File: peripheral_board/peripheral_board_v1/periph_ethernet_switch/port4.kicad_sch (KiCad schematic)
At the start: 7 parts, among them J4 0826-1G1T-23-F

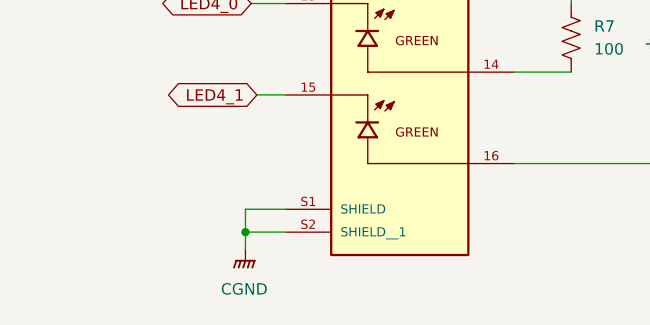
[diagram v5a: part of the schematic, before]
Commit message: Switch PCB layout done
The layout should be done. there are a lot of DRC errors but it seems like it is all for things like through holes and other similar items are causing this.
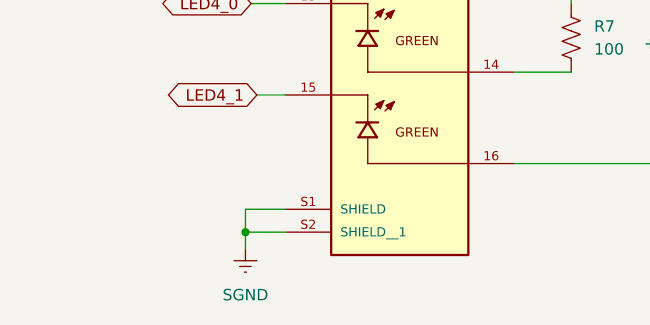
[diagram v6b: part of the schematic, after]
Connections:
- net CGND is gone; now on net SGND: J4.S1 (SHIELD), J4.S2 (SHIELD__1)
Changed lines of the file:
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@@
+	(symbol
+		(lib_id "power:GNDREF")
+		(at 42.545 87.63 0)
+		(unit 1)
+		(exclude_from_sim no)
+		(in_bom yes)
+		(on_board yes)
+		(dnp no)
+		(property "Reference" "#PWR028"
+			(at 42.545 93.98 0)
+			(effects
+				(font
+					(size 1.27 1.27)
+				)
+				(hide yes)
+			)
+		)
+		(property "Value" "SGND"
+			(at 42.545 92.71 0)
+			(effects
+				(font
+					(size 1.27 1.27)
+				)
+			)
+		)
+		(property "Footprint" ""
+			(at 42.545 87.63 0)
+			(effects
+				(font
+					(size 1.27 1.27)
+				)
+				(hide yes)
+			)
+		)
+		(property "Datasheet" ""
+			(at 42.545 87.63 0)
+			(effects
+				(font
+					(size 1.27 1.27)
+				)
+				(hide yes)
+			)
+		)
+		(property "Description" "Power symbol creates a global label with name \"GNDREF\" , reference supply ground"
+			(at 42.545 87.63 0)
+			(effects
+				(font
+					(size 1.27 1.27)
+				)
+				(hide yes)
+			)
+		)
+		(pin "1"
+		)
+		(instances
+			(project "periph_ethernet_switch"
+				(path "/065aff9d-de72-4d05-9bf8-aade8202d5c4/c3ca900e-99ac-4769-98db-f2b6577cf32c"
+					(reference "#PWR028")
+					(unit 1)
+				)
+			)
+		)
+	)
 	(symbol
 		(lib_id "power:GNDREF")
@@
 					(unit 1)
 				)
-			)
-		)
-	)
-	(symbol
-		(lib_id "power:GNDPWR")
-		(at 42.545 87.63 0)
-		(unit 1)
-		(exclude_from_sim no)
-		(in_bom yes)
-		(on_board yes)
-		(dnp no)
-		(fields_autoplaced yes)
-		(property "Reference" "#PWR035"
-			(at 42.545 92.71 0)
-			(effects
-				(font
-					(size 1.27 1.27)
-				)
-				(hide yes)
-			)
-		)
-		(property "Value" "CGND"
-			(at 42.418 92.075 0)
-			(effects
-				(font
-					(size 1.27 1.27)
-				)
-			)
-		)
-		(property "Footprint" ""
-			(at 42.545 88.9 0)
-			(effects
-				(font
-					(size 1.27 1.27)
-				)
-				(hide yes)
-			)
-		)
-		(property "Datasheet" ""
-			(at 42.545 88.9 0)
-			(effects
-				(font
-					(size 1.27 1.27)
-				)
-				(hide yes)
-			)
-		)
-		(property "Description" "Power symbol creates a global label with name \"CGND\" , CHASSIS GND"
-			(at 42.545 87.63 0)
-			(effects
-				(font
-					(size 1.27 1.27)
-				)
-				(hide yes)
-			)
-		)
-		(pin "1"
-		)
-		(instances
-			(project "periph_ethernet_switch"
-				(path "/065aff9d-de72-4d05-9bf8-aade8202d5c4/c3ca900e-99ac-4769-98db-f2b6577cf32c"
-					(reference "#PWR035")
-					(unit 1)
-				)

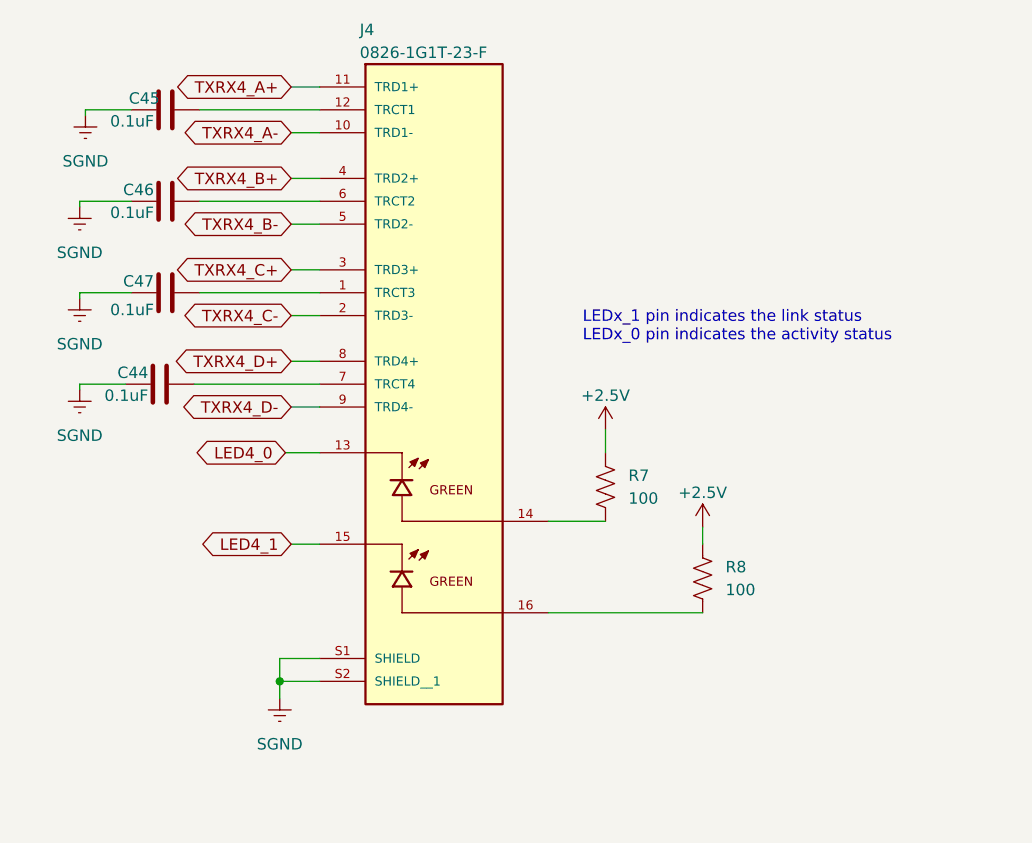
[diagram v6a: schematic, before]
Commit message: WIP for new switch
Made some minor changes which are detailed in Notion.
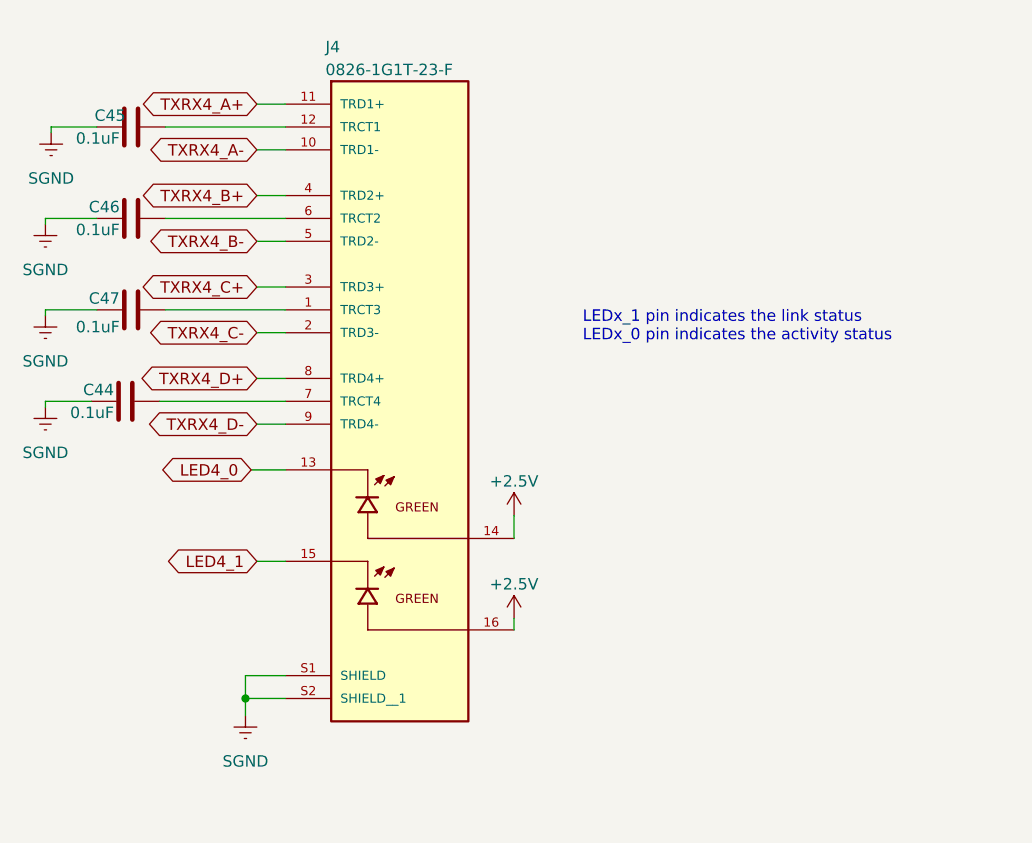
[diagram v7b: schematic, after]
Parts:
- removed R7, R8: 100, Resistor_SMD:R_0603_1608Metric, symbol Device:R_US
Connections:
- net +2.5V: now also J4.14, J4.16
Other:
- moved on the sheet: C44, C45, C46, C47, J4

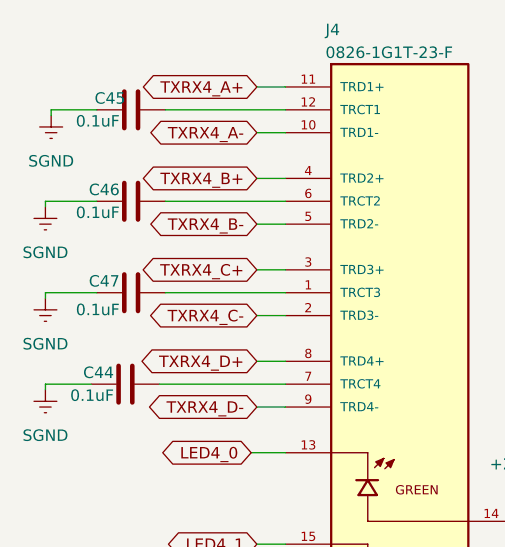
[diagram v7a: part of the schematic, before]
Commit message: Changes to the board layout
Need to finish doing some layout but waiting on Microchip to confirm with what I have. Might want to change the EDA symbol for the switch IC.
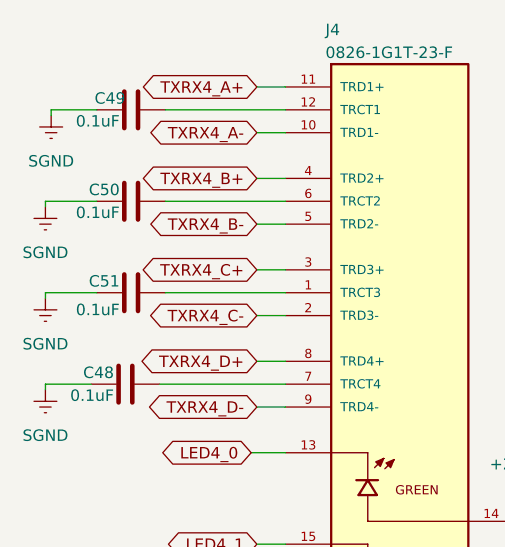
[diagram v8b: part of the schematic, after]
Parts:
- renumbered C44 to C48, C45 to C49, C46 to C50, C47 to C51
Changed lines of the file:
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@@
 		(on_board yes)
 		(dnp no)
-		(property "Reference" "#PWR033"
+		(property "Reference" "#PWR081"
 			(at 16.51 61.595 0)
 			(effects
@@
 			(project "periph_ethernet_switch"
 				(path "/065aff9d-de72-4d05-9bf8-aade8202d5c4/c3ca900e-99ac-4769-98db-f2b6577cf32c"
-					(reference "#PWR033")
+					(reference "#PWR081")
 					(unit 1)
 				)
@@
 		(on_board yes)
 		(dnp no)
-		(property "Reference" "C45"
+		(property "Reference" "C49"
 			(at 25.4 22.86 90)
 			(effects
@@
 			(project "periph_ethernet_switch"
 				(path "/065aff9d-de72-4d05-9bf8-aade8202d5c4/c3ca900e-99ac-4769-98db-f2b6577cf32c"
-					(reference "C45")
+					(reference "C49")
 					(unit 1)
 				)
@@
 		(on_board yes)
 		(dnp no)
-		(property "Reference" "C46"
+		(property "Reference" "C50"
 			(at 24.765 33.02 90)
 			(effects
@@
 			(project "periph_ethernet_switch"
 				(path "/065aff9d-de72-4d05-9bf8-aade8202d5c4/c3ca900e-99ac-4769-98db-f2b6577cf32c"
-					(reference "C46")
+					(reference "C50")
 					(unit 1)
 				)
@@
 		(on_board yes)
 		(dnp no)
-		(property "Reference" "#PWR028"
+		(property "Reference" "#PWR083"
 			(at 38.735 95.885 0)
 			(effects
@@
 			(project "periph_ethernet_switch"
 				(path "/065aff9d-de72-4d05-9bf8-aade8202d5c4/c3ca900e-99ac-4769-98db-f2b6577cf32c"
-					(reference "#PWR028")
+					(reference "#PWR083")
 					(unit 1)
 				)
@@
 		(on_board yes)
 		(dnp no)
-		(property "Reference" "#PWR034"
+		(property "Reference" "#PWR082"
 			(at 17.145 31.115 0)
 			(effects
@@
 			(project "periph_ethernet_switch"
 				(path "/065aff9d-de72-4d05-9bf8-aade8202d5c4/c3ca900e-99ac-4769-98db-f2b6577cf32c"
-					(reference "#PWR034")
+					(reference "#PWR082")
 					(unit 1)
 				)
@@
 		(on_board yes)
 		(dnp no)
-		(property "Reference" "#PWR031"
+		(property "Reference" "#PWR079"
 			(at 16.51 41.275 0)
 			(effects
@@
 			(project "periph_ethernet_switch"
 				(path "/065aff9d-de72-4d05-9bf8-aade8202d5c4/c3ca900e-99ac-4769-98db-f2b6577cf32c"
-					(reference "#PWR031")
+					(reference "#PWR079")
 					(unit 1)
 				)
@@
 		(on_board yes)
 		(dnp no)
-		(property "Reference" "C47"
+		(property "Reference" "C51"
 			(at 24.765 43.18 90)
 			(effects
@@
 			(project "periph_ethernet_switch"
 				(path "/065aff9d-de72-4d05-9bf8-aade8202d5c4/c3ca900e-99ac-4769-98db-f2b6577cf32c"
-					(reference "C47")
+					(reference "C51")
 					(unit 1)
 				)
@@
 		(on_board yes)
 		(dnp no)
-		(property "Reference" "#PWR036"
+		(property "Reference" "#PWR084"
 			(at 68.58 71.12 0)
 			(effects
@@
 			(project "periph_ethernet_switch"
 				(path "/065aff9d-de72-4d05-9bf8-aade8202d5c4/c3ca900e-99ac-4769-98db-f2b6577cf32c"
-					(reference "#PWR036")
+					(reference "#PWR084")
 					(unit 1)
 				)
@@
 		(on_board yes)
 		(dnp no)
-		(property "Reference" "#PWR032"
+		(property "Reference" "#PWR080"
 			(at 16.51 51.435 0)
 			(effects
@@
 			(project "periph_ethernet_switch"
 				(path "/065aff9d-de72-4d05-9bf8-aade8202d5c4/c3ca900e-99ac-4769-98db-f2b6577cf32c"
-					(reference "#PWR032")
+					(reference "#PWR080")
 					(unit 1)
 				)
@@
 		(on_board yes)
 		(dnp no)
-		(property "Reference" "#PWR037"
+		(property "Reference" "#PWR085"
 			(at 68.58 82.55 0)
 			(effects
@@
 			(project "periph_ethernet_switch"
 				(path "/065aff9d-de72-4d05-9bf8-aade8202d5c4/c3ca900e-99ac-4769-98db-f2b6577cf32c"
-					(reference "#PWR037")
+					(reference "#PWR085")
 					(unit 1)
 				)
@@
 		(on_board yes)
 		(dnp no)
-		(property "Reference" "C44"
+		(property "Reference" "C48"
 			(at 24.13 53.34 90)
 			(effects
@@
 			(project "periph_ethernet_switch"
 				(path "/065aff9d-de72-4d05-9bf8-aade8202d5c4/c3ca900e-99ac-4769-98db-f2b6577cf32c"
-					(reference "C44")
-					(unit 1)
-				)
+					(reference "C48")
+					(unit 1)
+				)
